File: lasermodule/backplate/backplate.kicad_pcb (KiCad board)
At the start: 2 copper layers, 33.2 x 64.1 mm, 2 parts

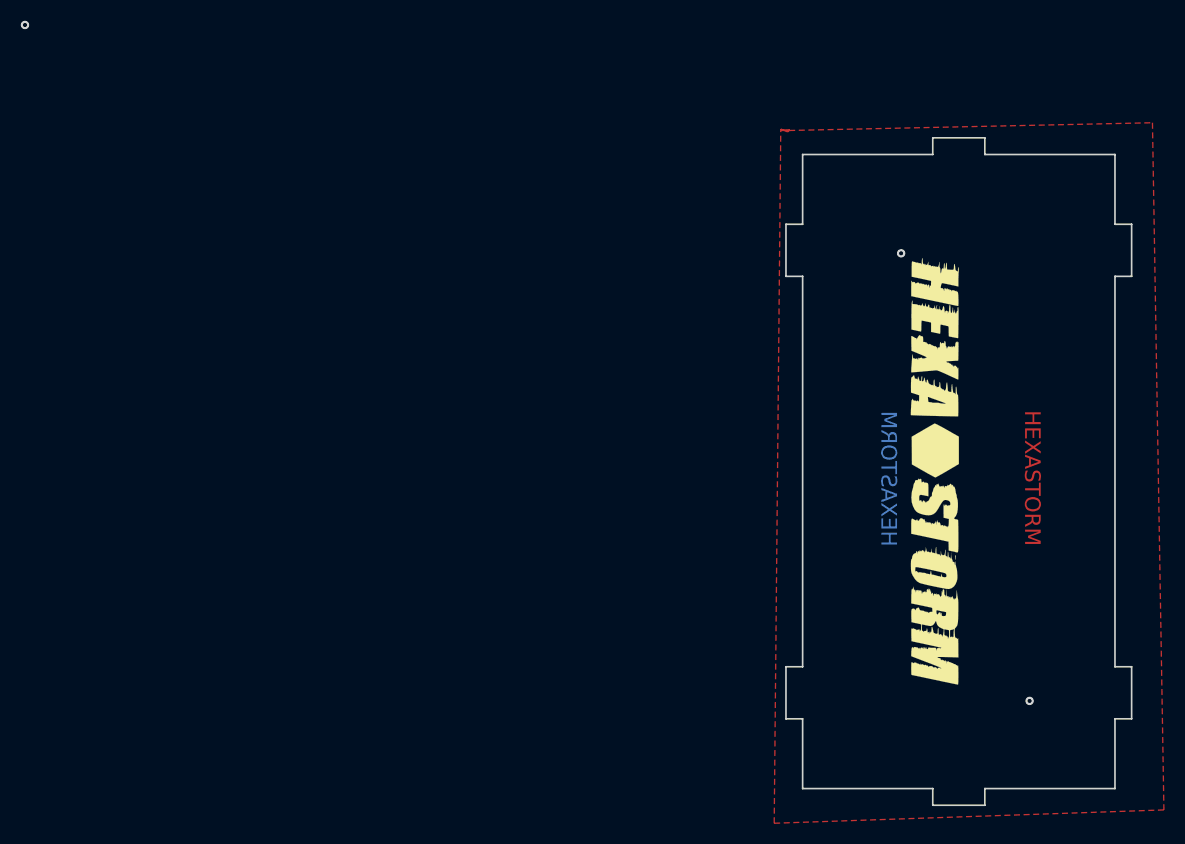
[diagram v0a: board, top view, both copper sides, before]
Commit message: removed need for screws using pcb pads
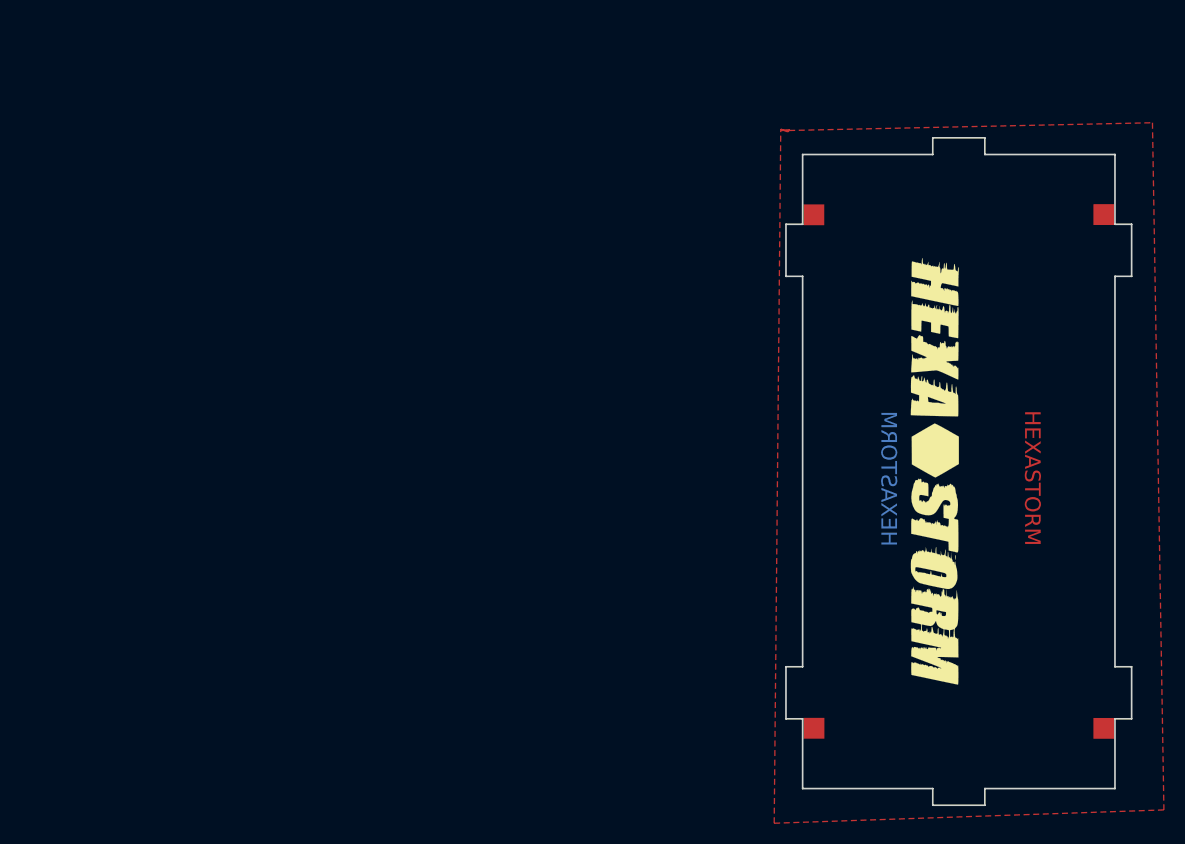
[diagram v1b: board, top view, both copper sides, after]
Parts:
- added J1: Conn_01x01, footprints:TestPoint_Pad_2.0x2.0mm_nosilk, F.Cu at (140.2, 79.3)
- added J2: Conn_01x01, footprints:TestPoint_Pad_2.0x2.0mm_nosilk, F.Cu at (168.0, 79.3)
- added J3: Conn_01x01, footprints:TestPoint_Pad_2.0x2.0mm_nosilk, F.Cu at (168.0, 128.6)
- added J4: Conn_01x01, footprints:TestPoint_Pad_2.0x2.0mm_nosilk, F.Cu at (140.2, 128.6)
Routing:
- net (no net): vias 3 -> 0
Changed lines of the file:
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@@
   )
   (net 0 "")
+  (net 1 "unconnected-(J1-Pin_1-Pad1)")
+  (net 2 "unconnected-(J2-Pin_1-Pad1)")
+  (net 3 "unconnected-(J3-Pin_1-Pad1)")
+  (net 4 "unconnected-(J4-Pin_1-Pad1)")
   (footprint "footprints:hexastorm" (layer "F.Cu")
     (at 151.83134 103.886 -90)
+    (property "Sheetfile" "backplate.kicad_sch")
+    (property "Sheetname" "")
+    (property "ki_description" "Open Hardware logo, large")
+    (property "ki_keywords" "Logo")
     (attr through_hole)
     (fp_text reference "L1" (at -0.67818 0.92964 90) (layer "F.SilkS") hide
@@
       (stroke (width 0.01) (type solid)) (fill solid) (layer "F.SilkS"))
   )
+  (footprint "footprints:TestPoint_Pad_2.0x2.0mm_nosilk" (layer "F.Cu")
+    (at 168.0445 128.6195)
+    (descr "SMD rectangular pad as test Point, square 2.0mm side length")
+    (tags "test point SMD pad rectangle square")
+    (property "Sheetfile" "backplate.kicad_sch")
+    (property "Sheetname" "")
+    (property "ki_description" "Generic connector, single row, 01x01, script generated (kicad-library-utils/schlib/autogen/connector/)")
+    (property "ki_keywords" "connector")
+    (attr exclude_from_pos_files)
+    (fp_text reference "J3" (at 0 -1.998) (layer "F.SilkS") hide
+        (effects (font (size 1 1) (thickness 0.15)))
+    )
+    (fp_text value "Conn_01x01" (at 0 2.05) (layer "F.Fab")
+        (effects (font (size 1 1) (thickness 0.15)))
+    )
+    (fp_text user "${REFERENCE}" (at 0 -2) (layer "F.Fab")
+        (effects (font (size 1 1) (thickness 0.15)))
+    )
+    (fp_line (start -1.5 -1.5) (end -1.5 1.5)
+      (stroke (width 0.05) (type solid)) (layer "F.CrtYd"))
+    (fp_line (start -1.5 -1.5) (end 1.5 -1.5)
+      (stroke (width 0.05) (type solid)) (layer "F.CrtYd"))
+    (fp_line (start 1.5 1.5) (end -1.5 1.5)
+      (stroke (width 0.05) (type solid)) (layer "F.CrtYd"))
+    (fp_line (start 1.5 1.5) (end 1.5 -1.5)
+      (stroke (width 0.05) (type solid)) (layer "F.CrtYd"))
+    (pad "1" smd rect (at 0 0) (size 2 2) (layers "F.Cu" "F.Mask")
+      (net 3 "unconnected-(J3-Pin_1-Pad1)") (pinfunction "Pin_1") (pintype "passive+no_connect"))
+  )
+  (footprint "footprints:TestPoint_Pad_2.0x2.0mm_nosilk" (layer "F.Cu")
+    (at 140.2045 128.6095)
+    (descr "SMD rectangular pad as test Point, square 2.0mm side length")
+    (tags "test point SMD pad rectangle square")
+    (property "Sheetfile" "backplate.kicad_sch")
+    (property "Sheetname" "")
+    (property "ki_description" "Generic connector, single row, 01x01, script generated (kicad-library-utils/schlib/autogen/connector/)")
+    (property "ki_keywords" "connector")
+    (attr exclude_from_pos_files)
+    (fp_text reference "J4" (at 0 -1.998) (layer "F.SilkS") hide
+        (effects (font (size 1 1) (thickness 0.15)))
+    )
+    (fp_text value "Conn_01x01" (at 0 2.05) (layer "F.Fab")
+        (effects (font (size 1 1) (thickness 0.15)))
+    )
+    (fp_text user "${REFERENCE}" (at 0 -2) (layer "F.Fab")
+        (effects (font (size 1 1) (thickness 0.15)))
+    )
+    (fp_line (start -1.5 -1.5) (end -1.5 1.5)
+      (stroke (width 0.05) (type solid)) (layer "F.CrtYd"))
+    (fp_line (start -1.5 -1.5) (end 1.5 -1.5)
+      (stroke (width 0.05) (type solid)) (layer "F.CrtYd"))
+    (fp_line (start 1.5 1.5) (end -1.5 1.5)
+      (stroke (width 0.05) (type solid)) (layer "F.CrtYd"))
+    (fp_line (start 1.5 1.5) (end 1.5 -1.5)
+      (stroke (width 0.05) (type solid)) (layer "F.CrtYd"))
+    (pad "1" smd rect (at 0 0) (size 2 2) (layers "F.Cu" "F.Mask")
+      (net 4 "unconnected-(J4-Pin_1-Pad1)") (pinfunction "Pin_1") (pintype "passive+no_connect"))
+  )
+  (footprint "footprints:TestPoint_Pad_2.0x2.0mm_nosilk" (layer "F.Cu")
+    (at 140.1945 79.2895)
+    (descr "SMD rectangular pad as test Point, square 2.0mm side length")
+    (tags "test point SMD pad rectangle square")
+    (property "Sheetfile" "backplate.kicad_sch")
+    (property "Sheetname" "")
+    (property "ki_description" "Generic connector, single row, 01x01, script generated (kicad-library-utils/schlib/autogen/connector/)")
+    (property "ki_keywords" "connector")
+    (attr exclude_from_pos_files)
+    (fp_text reference "J1" (at 0 -1.998) (layer "F.SilkS") hide
+        (effects (font (size 1 1) (thickness 0.15)))
+    )
+    (fp_text value "Conn_01x01" (at 0 2.05) (layer "F.Fab")
+        (effects (font (size 1 1) (thickness 0.15)))
+    )
+    (fp_text user "${REFERENCE}" (at 0 -2) (layer "F.Fab")
+        (effects (font (size 1 1) (thickness 0.15)))
+    )
+    (fp_line (start -1.5 -1.5) (end -1.5 1.5)
+      (stroke (width 0.05) (type solid)) (layer "F.CrtYd"))
+    (fp_line (start -1.5 -1.5) (end 1.5 -1.5)
+      (stroke (width 0.05) (type solid)) (layer "F.CrtYd"))
+    (fp_line (start 1.5 1.5) (end -1.5 1.5)
+      (stroke (width 0.05) (type solid)) (layer "F.CrtYd"))
+    (fp_line (start 1.5 1.5) (end 1.5 -1.5)
+      (stroke (width 0.05) (type solid)) (layer "F.CrtYd"))
+    (pad "1" smd rect (at 0 0) (size 2 2) (layers "F.Cu" "F.Mask")
+      (net 1 "unconnected-(J1-Pin_1-Pad1)") (pinfunction "Pin_1") (pintype "passive+no_connect"))
+  )
+  (footprint "footprints:TestPoint_Pad_2.0x2.0mm_nosilk" (layer "F.Cu")
+    (at 168.0445 79.2695)
+    (descr "SMD rectangular pad as test Point, square 2.0mm side length")
+    (tags "test point SMD pad rectangle square")
+    (property "Sheetfile" "backplate.kicad_sch")
+    (property "Sheetname" "")
+    (property "ki_description" "Generic connector, single row, 01x01, script generated (kicad-library-utils/schlib/autogen/connector/)")
+    (property "ki_keywords" "connector")
+    (attr exclude_from_pos_files)
+    (fp_text reference "J2" (at 0 -1.998) (layer "F.SilkS") hide
+        (effects (font (size 1 1) (thickness 0.15)))
+    )
+    (fp_text value "Conn_01x01" (at 0 2.05) (layer "F.Fab")
+        (effects (font (size 1 1) (thickness 0.15)))
+    )
+    (fp_text user "${REFERENCE}" (at 0 -2) (layer "F.Fab")
+        (effects (font (size 1 1) (thickness 0.15)))
+    )
+    (fp_line (start -1.5 -1.5) (end -1.5 1.5)
+      (stroke (width 0.05) (type solid)) (layer "F.CrtYd"))
+    (fp_line (start -1.5 -1.5) (end 1.5 -1.5)
+      (stroke (width 0.05) (type solid)) (layer "F.CrtYd"))
+    (fp_line (start 1.5 1.5) (end -1.5 1.5)
+      (stroke (width 0.05) (type solid)) (layer "F.CrtYd"))
+    (fp_line (start 1.5 1.5) (end 1.5 -1.5)
+      (stroke (width 0.05) (type solid)) (layer "F.CrtYd"))
+    (pad "1" smd rect (at 0 0) (size 2 2) (layers "F.Cu" "F.Mask")
+      (net 2 "unconnected-(J2-Pin_1-Pad1)") (pinfunction "Pin_1") (pintype "passive+no_connect"))
+  )
   (footprint "footprints:hexastorm" (layer "B.Cu")
     (at 151.83134 104.43464 90)
+    (property "Sheetfile" "backplate.kicad_sch")
+    (property "Sheetname" "")
+    (property "ki_description" "Open Hardware logo, large")
+    (property "ki_keywords" "Logo")
     (attr through_hole)
     (fp_text reference "L2" (at 0 0 90) (layer "B.SilkS") hide
@@
     (effects (font (size 1 1) (thickness 0.15)) (justify left bottom))
   )
-  (via (at 148.5745 82.9895) (size 0.8) (drill 0.4) (layers "F.Cu" "B.Cu") (free) (net 0))
-  (via (at 160.9145 125.9795) (size 0.8) (drill 0.4) (layers "F.Cu" "B.Cu") (free) (net 0))
-  (via (at 64.4245 61.0595) (size 0.8) (drill 0.4) (layers "F.Cu" "B.Cu") (free) (net 0))
   (zone (net 0) (net_name "") (layer "F.Cu") (hatch edge 0.508)
     (connect_pads (clearance 0.508))

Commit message: board almost fully synced close for release
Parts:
- removed L1, L2: Logo_Open_Hardware_Large, footprints:hexastorm
- added J5: Conn_01x02, footprints:pogopincontact, F.Cu at (156.7, 103.9)
- moved J2 9.15 mm to (164.6, 87.7), turned to 90 degrees
- moved J1 9.13 mm to (143.6, 87.7), turned to 90 degrees
- moved J3 9.05 mm to (164.6, 120.2), turned to 90 degrees
- moved J4 9.03 mm to (143.6, 120.2), turned to -90 degrees
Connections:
- J1 pad 1: unconnected-(J1-Pin_1-Pad1) -> +12V
- J4 pad 1: unconnected-(J4-Pin_1-Pad1) -> LDK
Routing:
- net +12V: track 0.00 -> 32.6 mm, vias 0 -> 2
- net LDK: track 0.00 -> 31.9 mm, vias 0 -> 2
- added copper zone on B.Cu, net LDK
- added copper zone on F.Cu, net LDK
- removed copper zone on F.Cu, net (none)
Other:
- board size 33.2 x 64.1 mm -> 24.2 x 54.1 mm
- board text removed: "HEXASTORM"

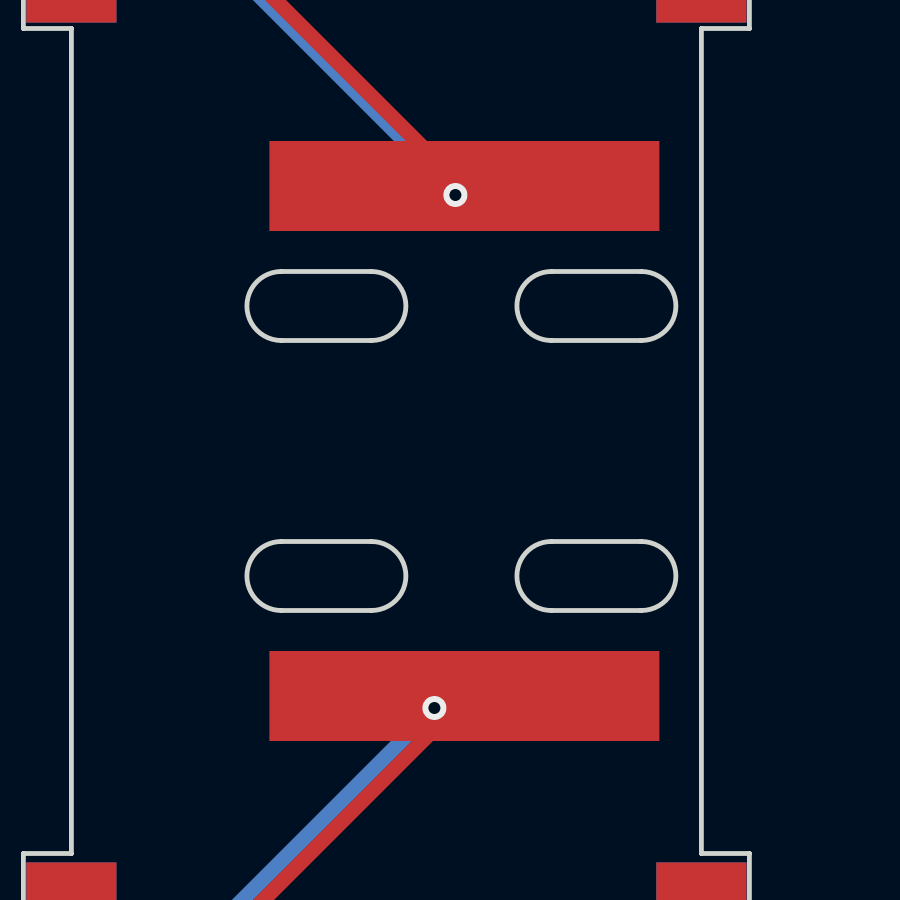
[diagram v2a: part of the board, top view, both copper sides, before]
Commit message: added kicost tracking other plates, fixed plates
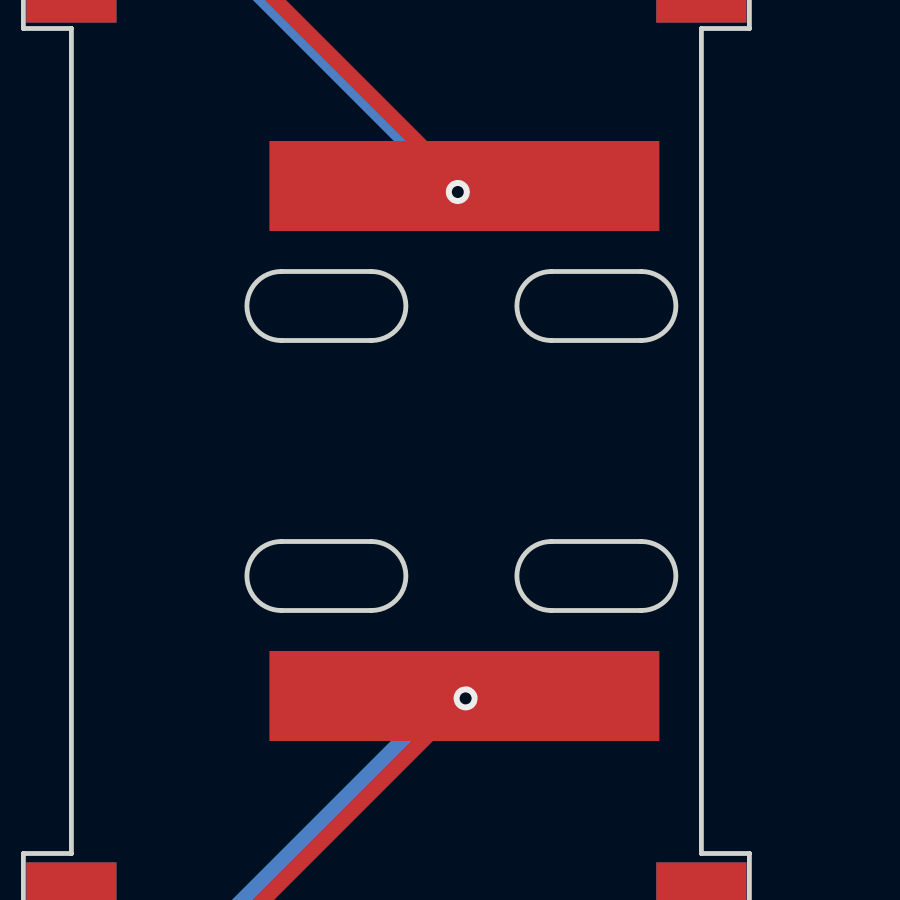
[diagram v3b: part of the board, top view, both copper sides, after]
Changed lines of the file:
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@@
 	)
 	(via
-		(at 156.4145 95.7495)
+		(at 156.4945 95.6495)
 		(size 0.8)
 		(drill 0.4)
@@
 	)
 	(via
-		(at 155.7145 112.8495)
+		(at 156.7545 112.5295)
 		(size 0.8)
 		(drill 0.4)

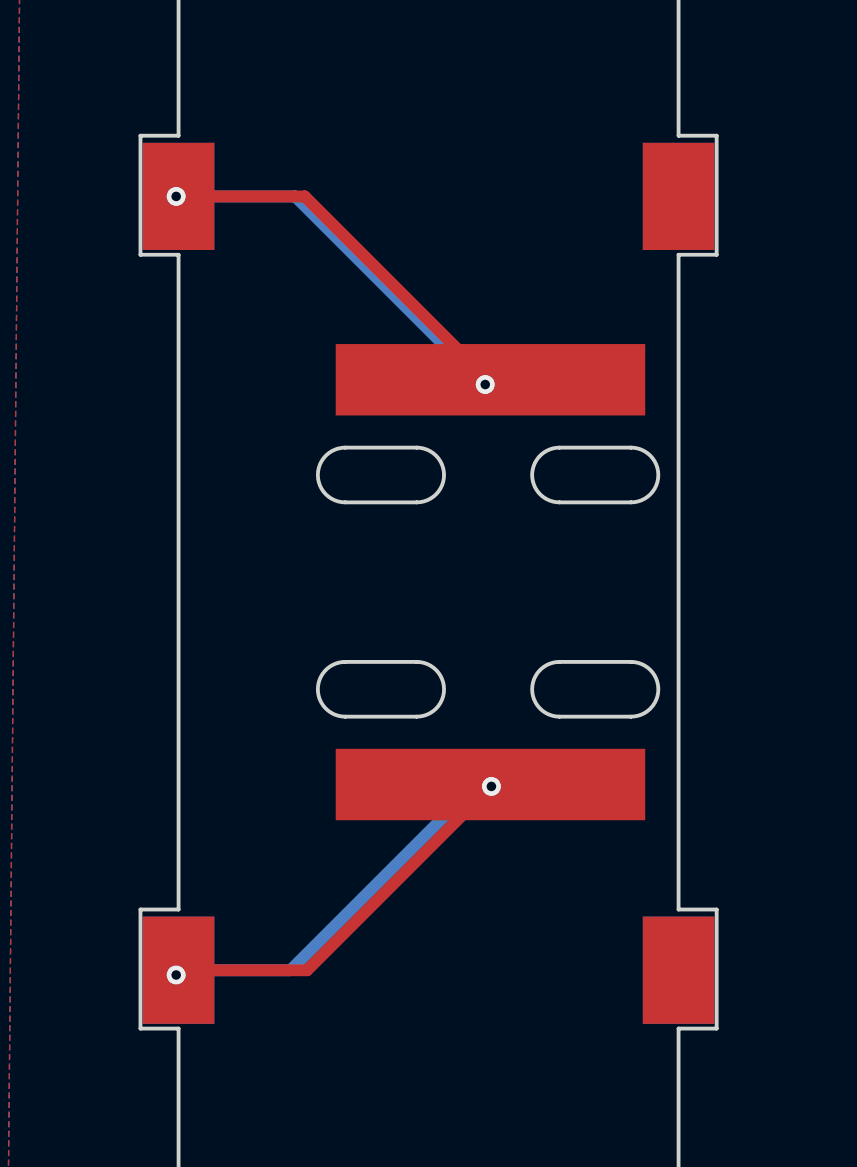
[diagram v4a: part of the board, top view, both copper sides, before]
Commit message: changes to reduce prices pcbway
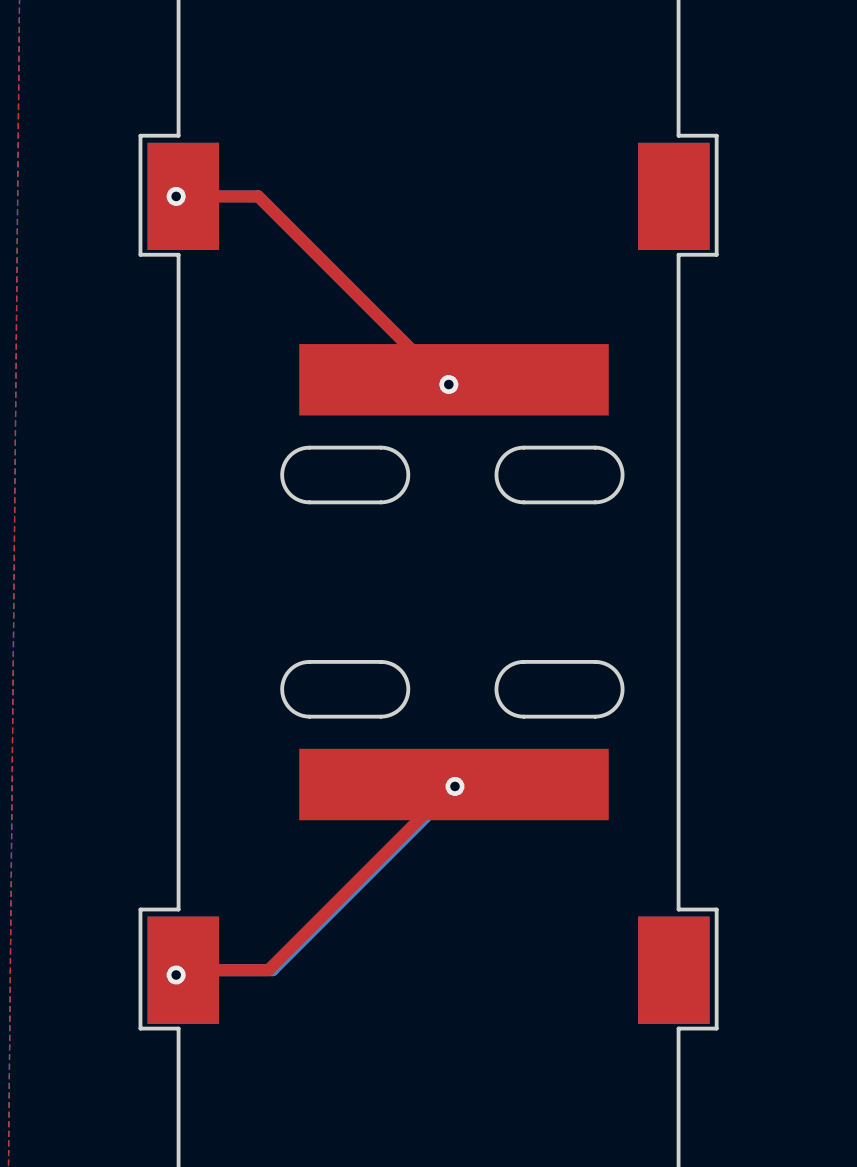
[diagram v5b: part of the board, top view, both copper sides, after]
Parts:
- moved J5 1.53 mm to (155.2, 103.9)
- moved J1 0.20 mm to (143.8, 87.7)
- moved J4 0.20 mm to (143.8, 120.2)
- moved J2 0.20 mm to (164.4, 87.7)
- moved J3 0.20 mm to (164.4, 120.2)
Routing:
- net +12V: track 32.6 -> 29.1 mm
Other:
- outline, holes or cut-outs redrawn

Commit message: sent to pcbway
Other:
- board text added: "12V"
- board text added: "LDK"
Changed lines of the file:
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@@
 		(layer "Edge.Cuts")
+	)
+	(gr_text "12V"
+		(at 153.7645 88.3745 -90)
+		(layer "F.SilkS")
+		(effects
+			(font
+				(size 1.5 1.5)
+				(thickness 0.3)
+				(bold yes)
+			)
+			(justify left bottom)
+		)
+	)
+	(gr_text "LDK"
+		(at 154.3645 114.7745 270)
+		(layer "F.SilkS")
+		(effects
+			(font
+				(size 1.5 1.5)
+				(thickness 0.3)
+				(bold yes)
+			)
+			(justify left bottom)
+		)
 	)
 	(gr_text "PCB3D_BR_backplate"
